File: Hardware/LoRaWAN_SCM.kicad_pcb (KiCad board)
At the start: 4 copper layers, 101.8 x 57.8 mm, 73 parts, among them J1 Conn_02x05_Odd_Even, J10 Conn_02x06_Odd_Even, J2 Conn_02x05_Odd_Even, J3 Screw_Terminal_01x02, J4 Screw_Terminal_01x03, J5 Conn_Coaxial, J6 Screw_Terminal_01x03, J7 Conn_02x06_Odd_Even, J8 Conn_02x06_Odd_Even, J9 Conn_02x06_Odd_Even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

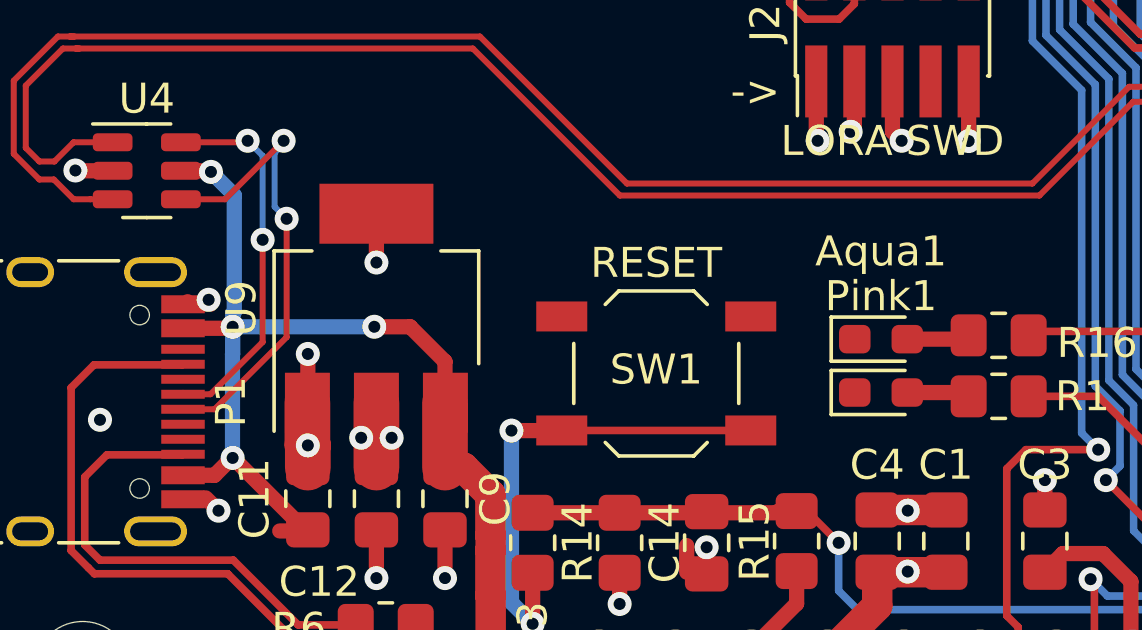
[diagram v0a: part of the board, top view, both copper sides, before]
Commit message: updated arduino code and fixed usb isuue on pcb
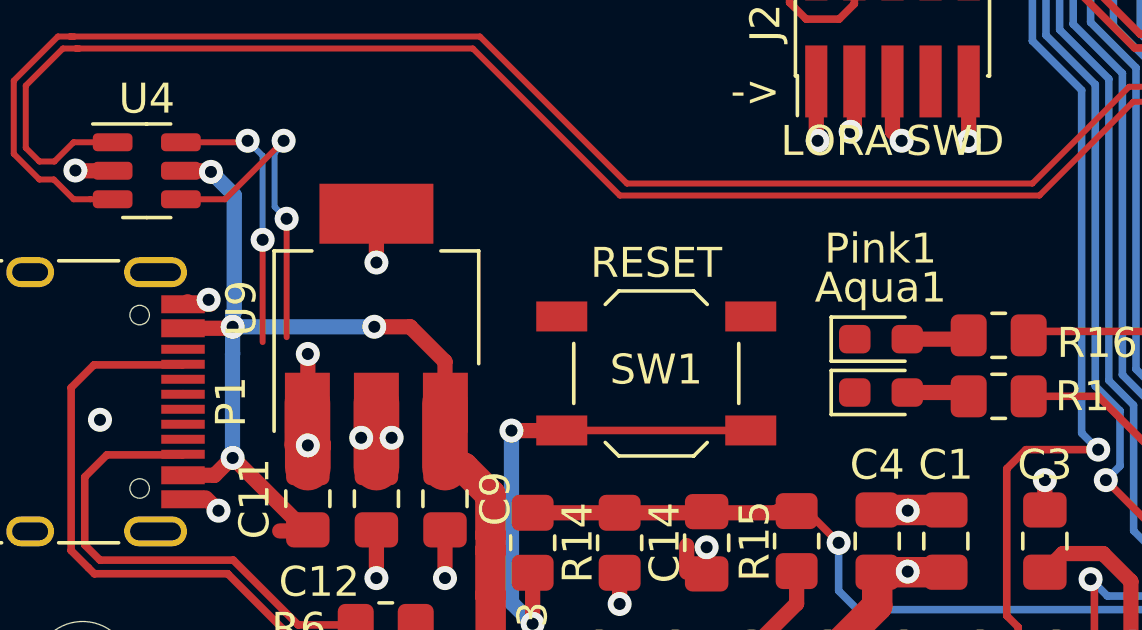
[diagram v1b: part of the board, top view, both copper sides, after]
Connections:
- R5 pad 1: Net-(P1-PadA5) -> Net-(R5-Pad1)
- R6 pad 1: Net-(P1-PadB5) -> Net-(R6-Pad1)
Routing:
- net D-: track 15.5 -> 11.1 mm
- net D+: track 12.6 -> 9.23 mm
